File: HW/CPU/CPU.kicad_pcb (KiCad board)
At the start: 2 copper layers, 13 parts, among them J1 I2C, J2 SBW, J3 PWR, U1 CONRAD_USB_UART, U2 MSP430G2452, X1 XTAL

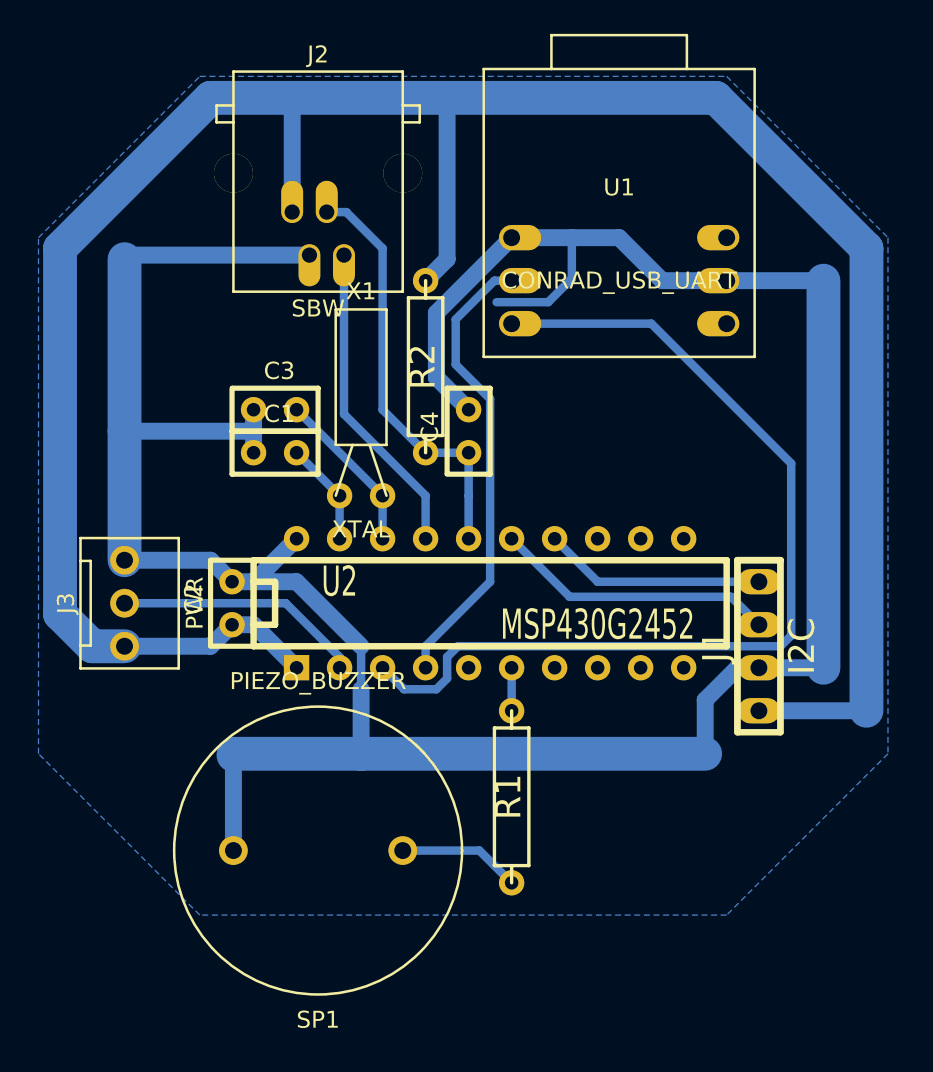
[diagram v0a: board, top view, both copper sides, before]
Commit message: CPU board: PCB Design improvement (incomplette)
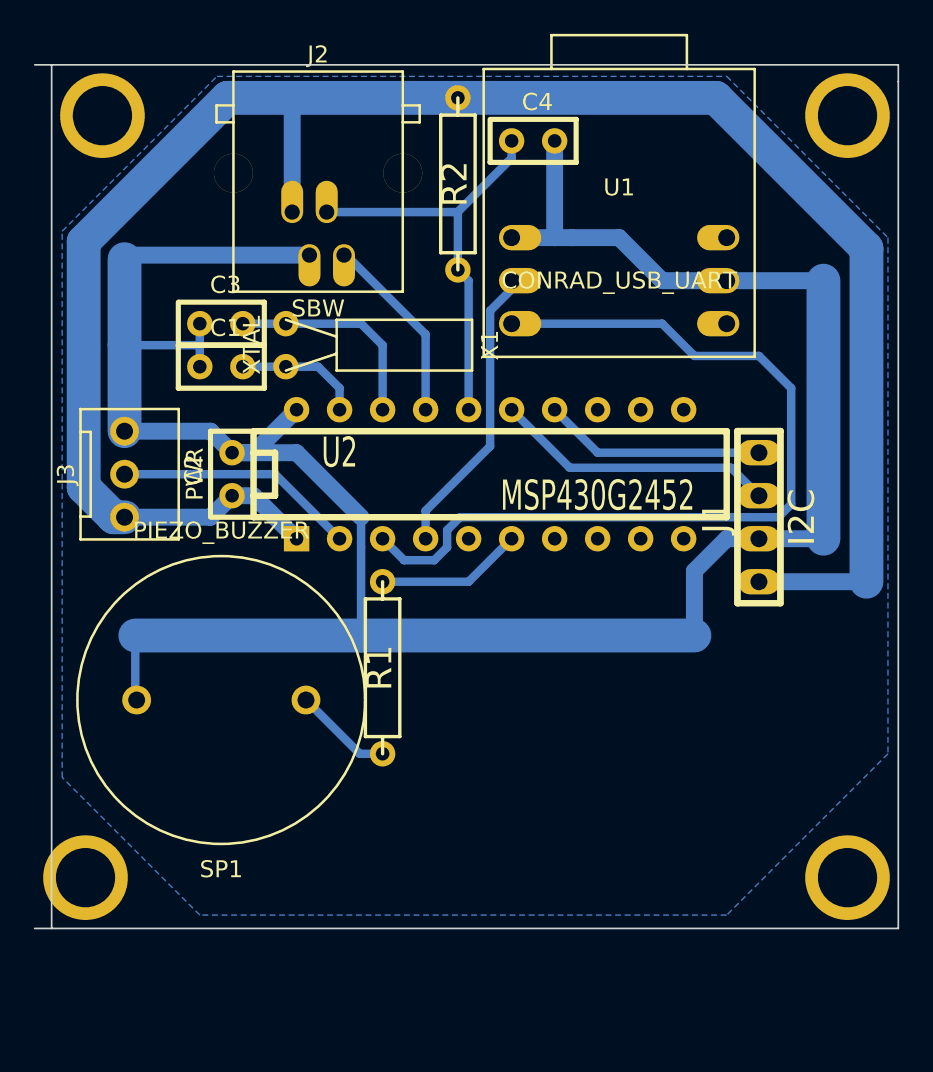
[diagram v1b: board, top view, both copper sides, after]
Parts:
- added MNT_HOLE_3.5S: Val**, MNT_HOLE_3.5S, F.Cu at (197.0, 109.0)
- added MNT_HOLE_3.5S: Val**, MNT_HOLE_3.5S, F.Cu at (197.0, 154.0)
- added MNT_HOLE_3.5S: Val**, MNT_HOLE_3.5S, F.Cu at (152.0, 154.0)
- added MNT_HOLE_3.5S: Val**, MNT_HOLE_3.5S, F.Cu at (153.0, 109.0)
- moved C4 17.6 mm to (178.4, 110.5), turned to 0 degrees
- moved R2 11.0 mm to (174.0, 113.0)
- moved R1 10.8 mm to (169.5, 141.6)
- moved SP1 10.6 mm to (160.0, 143.5)
- moved X1 9.94 mm to (163.8, 122.6), turned to 270 degrees
- moved J1 7.62 mm to (191.8, 132.7)
- moved C2 7.62 mm to (160.7, 130.2)
- moved J3 7.62 mm to (154.3, 130.2)
- moved U2 7.62 mm to (175.9, 130.2)
- moved C1 5.99 mm to (160.0, 123.8)
- moved C3 5.99 mm to (160.0, 121.3)
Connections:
- X1 pad 1: N-0000013 -> N-0000014
- X1 pad 2: N-0000014 -> N-0000013
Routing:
- net VCC: track 144.9 -> 115.8 mm
- net GND: track 172.1 -> 145.7 mm
- net N-0000012: track 27.2 -> 18.1 mm
- net N-000002: track 18.7 -> 11.4 mm
- net N-000005: track 2.54 -> 8.67 mm
- net N-000009: track 56.8 -> 51.6 mm
- net N-0000014: track 9.72 -> 12.6 mm
- net N-0000013: track 6.13 -> 7.51 mm
- net N-000004: track 7.22 -> 5.84 mm
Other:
- board outline added: 51 x 51 mm

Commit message: CPU board space optimization
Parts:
- moved R1 7.62 mm to (177.2, 141.6)
- moved SP1 5.12 mm to (165.1, 144.1)
- moved MNT_HOLE_3.5S 4.12 mm to (153.0, 150.0)
- moved MNT_HOLE_3.5S 4.00 mm to (197.0, 150.0)
- moved C4 3.18 mm to (178.4, 113.7)
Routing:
- net GND: track 145.7 -> 138.2 mm
- net N-000005: track 8.67 -> 2.54 mm
- net N-000004: track 5.84 -> 8.12 mm
- net N-000009: track 51.6 -> 49.6 mm
- net N-0000023: track 25.2 -> 23.3 mm
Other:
- board size 51 x 51 mm -> 50 x 47 mm
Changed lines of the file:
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@@
     (links 30)
     (no_connects 0)
-    (area 140.586934 101.4816 208.413066 163.229)
+    (area 141.586934 101.4816 208.413066 154.974)
     (thickness 1.6)
     (drawings 5)
-    (tracks 93)
+    (tracks 92)
     (zones 0)
     (modules 17)
@@
   )
   (module R4 (layer F.Cu)
-    (at 169.545 141.605 270)
+    (at 177.165 141.605 270)
     (descr "Resitance 4 pas")
     (tags R)
@@
   )
   (module PIEZO_BUZZER_D17 (layer F.Cu)
-    (at 160.02 143.51 180)
+    (at 165.1 144.145 180)
     (fp_text reference SP1 (at 0 -10 180) (layer F.SilkS)
       (effects (font (size 1 1) (thickness 0.15)))
@@
   )
   (module C1 (layer F.Cu)
-    (at 178.435 110.49)
+    (at 178.435 113.665)
     (descr "Condensateur e = 1 pas")
     (tags C)
@@
   )
   (module MNT_HOLE_3.5S (layer F.Cu)
-    (at 197 154)
+    (at 197 150)
     (fp_text reference MNT_HOLE_3.5S (at 0 -6.35) (layer F.SilkS) hide
       (effects (font (size 1.524 1.524) (thickness 0.3048)))
@@
   )
   (module MNT_HOLE_3.5S (layer F.Cu)
-    (at 152 154)
+    (at 153 150)
     (fp_text reference MNT_HOLE_3.5S (at 0 -6.35) (layer F.SilkS) hide
       (effects (font (size 1.524 1.524) (thickness 0.3048)))
@@
     )
   )
+  (gr_line (start 150 153) (end 150 106) (angle 90) (layer Edge.Cuts) (width 0.1))
+  (gr_line (start 200 153) (end 150 153) (angle 90) (layer Edge.Cuts) (width 0.1))
+  (gr_line (start 200 106) (end 200 153) (angle 90) (layer Edge.Cuts) (width 0.1))
+  (gr_line (start 150 106) (end 200 106) (angle 90) (layer Edge.Cuts) (width 0.1))
   (gr_line (start 200 106) (end 200 107) (angle 90) (layer Edge.Cuts) (width 0.1))
-  (gr_line (start 149 106) (end 200 106) (angle 90) (layer Edge.Cuts) (width 0.1))
-  (gr_line (start 150 157) (end 150 106) (angle 90) (layer Edge.Cuts) (width 0.1))
-  (gr_line (start 200 157) (end 149 157) (angle 90) (layer Edge.Cuts) (width 0.1))
-  (gr_line (start 200 107) (end 200 157) (angle 90) (layer Edge.Cuts) (width 0.1))
-  (segment (start 155.02 143.51) (end 154.94 143.43) (width 0.5) (layer B.Cu) (net 1) (status C00000))
-  (segment (start 154.94 139.7) (end 168.275 139.7) (width 2) (layer B.Cu) (net 1))
-  (segment (start 154.94 143.43) (end 154.94 139.7) (width 0.5) (layer B.Cu) (net 1) (status 400000))
+  (segment (start 160.1 144.145) (end 160.1 139.7) (width 0.5) (layer B.Cu) (net 1))
+  (segment (start 160.1 139.7) (end 160.02 139.7) (width 0.5) (layer B.Cu) (net 1))
+  (segment (start 160.02 139.7) (end 168.275 139.7) (width 2) (layer B.Cu) (net 1))
   (segment (start 168.275 139.7) (end 168.275 134.493) (width 0.5) (layer B.Cu) (net 1))
   (segment (start 168.275 132.715) (end 168.275 134.493) (width 0.5) (layer B.Cu) (net 1))
@@
   (segment (start 164.465 128.905) (end 168.275 132.715) (width 1) (layer B.Cu) (net 1))
   (segment (start 168.275 139.7) (end 187.96 139.7) (width 2) (layer B.Cu) (net 1))
-  (segment (start 189.865 133.985) (end 191.77 133.985) (width 1) (layer B.Cu) (net 1) (status 800000))
+  (segment (start 189.865 133.985) (end 191.77 133.985) (width 1) (layer B.Cu) (net 1))
   (segment (start 187.96 135.89) (end 187.96 139.7) (width 1) (layer B.Cu) (net 1))
   (segment (start 189.865 133.985) (end 187.96 135.89) (width 1) (layer B.Cu) (net 1))
@@
   (segment (start 158.75 121.285) (end 158.75 122.555) (width 0.5) (layer B.Cu) (net 1))
   (segment (start 158.75 122.555) (end 158.75 123.825) (width 0.5) (layer B.Cu) (net 1))
-  (segment (start 179.705 110.49) (end 179.705 116.205) (width 1) (layer B.Cu) (net 1))
+  (segment (start 179.705 113.665) (end 179.705 116.205) (width 1) (layer B.Cu) (net 1))
   (segment (start 180.721 116.205) (end 179.705 116.205) (width 1) (layer B.Cu) (net 1))
   (segment (start 186.055 118.745) (end 183.515 116.205) (width 1) (layer B.Cu) (net 1))
@@
   (segment (start 167.265 117.1) (end 172.085 121.92) (width 0.5) (layer B.Cu) (net 6))
   (segment (start 167.265 117.1) (end 167.265 117.235) (width 0.5) (layer B.Cu) (net 6))
+  (segment (start 173.99 114.709) (end 176.121 114.709) (width 0.5) (layer B.Cu) (net 7))
+  (segment (start 176.121 114.709) (end 177.165 113.665) (width 0.5) (layer B.Cu) (net 7))
   (segment (start 173.99 118.11) (end 174.625 118.745) (width 0.5) (layer B.Cu) (net 7))
   (segment (start 174.625 118.745) (end 174.625 126.365) (width 0.5) (layer B.Cu) (net 7))
@@
   (segment (start 173.99 114.709) (end 173.976 114.695) (width 0.5) (layer B.Cu) (net 7))
   (segment (start 166.245 114.695) (end 173.976 114.695) (width 0.5) (layer B.Cu) (net 7))
-  (segment (start 177.165 111.506) (end 177.165 110.49) (width 0.5) (layer B.Cu) (net 7))
-  (segment (start 173.976 114.695) (end 177.165 111.506) (width 0.5) (layer B.Cu) (net 7))
-  (segment (start 165.02 143.51) (end 168.195 146.685) (width 0.5) (layer B.Cu) (net 8) (status 400000))
-  (segment (start 168.195 146.685) (end 169.545 146.685) (width 0.5) (layer B.Cu) (net 8) (status 800000))
-  (segment (start 169.545 136.525) (end 174.625 136.525) (width 0.5) (layer B.Cu) (net 9) (status 400000))
-  (segment (start 174.625 136.525) (end 177.165 133.985) (width 0.5) (layer B.Cu) (net 9) (status 800000))
+  (segment (start 170.1 144.145) (end 174.625 144.145) (width 0.5) (layer B.Cu) (net 8))
+  (segment (start 174.625 144.145) (end 177.165 146.685) (width 0.5) (layer B.Cu) (net 8))
+  (segment (start 177.165 133.985) (end 177.165 136.525) (width 0.5) (layer B.Cu) (net 9))
   (segment (start 180.594 129.794) (end 177.165 126.365) (width 0.5) (layer B.Cu) (net 10))
   (segment (start 190.119 129.794) (end 180.594 129.794) (width 0.5) (layer B.Cu) (net 10))
@@
   (segment (start 172.593 135.255) (end 173.355 134.493) (width 0.5) (layer B.Cu) (net 12))
   (segment (start 170.815 135.255) (end 172.593 135.255) (width 0.5) (layer B.Cu) (net 12))
-  (segment (start 193.675 125.095) (end 193.675 131.953) (width 0.5) (layer B.Cu) (net 12))
-  (segment (start 186.055 121.285) (end 187.96 123.19) (width 0.5) (layer B.Cu) (net 12))
-  (segment (start 187.96 123.19) (end 191.77 123.19) (width 0.5) (layer B.Cu) (net 12))
-  (segment (start 191.77 123.19) (end 193.675 125.095) (width 0.5) (layer B.Cu) (net 12))
-  (segment (start 177.165 121.285) (end 186.055 121.285) (width 0.5) (layer B.Cu) (net 12))
+  (segment (start 193.675 128.397) (end 193.675 131.953) (width 0.5) (layer B.Cu) (net 12))
+  (segment (start 177.165 121.285) (end 180.848 124.968) (width 0.5) (layer B.Cu) (net 12))
+  (segment (start 180.848 124.968) (end 190.246 124.968) (width 0.5) (layer B.Cu) (net 12))
+  (segment (start 190.246 124.968) (end 193.675 128.397) (width 0.5) (layer B.Cu) (net 12))
+  (segment (start 177.165 121.285) (end 177.165 121.285) (width 0.5) (layer B.Cu) (net 12))
   (segment (start 192.913 132.715) (end 174.117 132.715) (width 0.5) (layer B.Cu) (net 12))
   (segment (start 193.675 131.953) (end 192.913 132.715) (width 0.5) (layer B.Cu) (net 12))
@@
     (polygon
       (pts
-        (xy 199.39 146.685) (xy 189.865 156.21) (xy 158.75 156.21) (xy 150.622 148.082) (xy 150.622 115.824)
+        (xy 199.39 142.875) (xy 189.865 152.4) (xy 160.147 152.4) (xy 150.622 142.875) (xy 150.622 115.824)
         (xy 159.766 106.68) (xy 189.865 106.68) (xy 199.39 116.205)
       )
